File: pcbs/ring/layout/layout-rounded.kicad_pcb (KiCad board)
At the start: 2 copper layers, 59.8 x 6.2 mm, 61 parts, among them J1 ?, Q1 CSD13380F3T, Q2 CSD13380F3T, U1 BQ27427YZFR, U2 BQ29700, U3 nRF52833-QDAA, U4 MAX30102EFD+T, U5 LSM6DSOX, U6 TMP117AIDRVR, U7 TPS7A2018PDQN, Y1 32MHz, Y2 32.768kHz

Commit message: rounded
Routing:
- net swdclk: track 46.0 -> 44.9 mm
- net swdio: track 37.4 -> 36.7 mm
- net cpu.dec4_6: track 18.2 -> 17.7 mm

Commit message: more vias
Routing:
- net GND: vias 50 -> 55

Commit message: cleanup
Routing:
- net GND: vias 55 -> 56
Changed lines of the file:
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@@
 	)
 	(via
+		(at 173.85 84.55)
+		(size 0.35)
+		(drill 0.15)
+		(layers "F.Cu" "B.Cu")
+		(free yes)
+		(net 2)
+	)
+	(via
 		(at 145.3 85.35)
 		(size 0.35)
@@
 	)
 	(segment
-		(start 139.172615 81.872615)
-		(end 138.673743 81.373743)
-		(width 0.125)
-		(layer "B.Cu")
-		(net 27)
-	)
-	(segment
 		(start 142.9 82.3)
 		(end 143.143933 82.3)
@@
 	)
 	(segment
-		(start 140.524819 83.2)
+		(start 139.172615 81.872615)
+		(end 138.673743 81.373743)
+		(width 0.125)
+		(layer "B.Cu")
+		(net 27)
+	)
+	(segment
+		(start 141.047805 83.2)
 		(end 141.075 83.2)
 		(width 0.125)
@@
 	)
 	(segment
-		(start 142.302512 82.547487)
-		(end 142.056586 82.793413)
+		(start 139.175385 81.879299)
+		(end 139.172615 81.872615)
 		(width 0.125)
 		(layer "B.Cu")
@@
 	)
 	(segment
-		(start 140.48245 83.18245)
-		(end 140.466283 83.166283)
+		(start 140.10596 82.809874)
+		(end 139.175385 81.879299)
+		(width 0.125)
+		(layer "B.Cu")
+		(net 27)
+	)
+	(segment
+		(start 142.302512 82.547487)
+		(end 142.056507 82.793492)
 		(width 0.125)
 		(layer "B.Cu")
@@
 		(net 27)
 	)
-	(segment
-		(start 140.459602 83.163516)
-		(end 139.175385 81.879299)
-		(width 0.125)
-		(layer "B.Cu")
-		(net 27)
-	)
-	(arc
-		(start 139.174 81.875957)
-		(mid 139.17436 81.877765)
-		(end 139.175385 81.879299)
-		(width 0.125)
-		(layer "B.Cu")
-		(net 27)
-	)
 	(arc
 		(start 147.84205 82.69205)
@@
 	)
 	(arc
-		(start 142.056586 82.793413)
-		(mid 141.60623 83.094331)
+		(start 142.056507 82.793492)
+		(mid 141.606238 83.094352)
 		(end 141.075 83.2)
 		(width 0.125)
@@
 	)
 	(arc
-		(start 140.459602 83.163516)
-		(mid 140.461134 83.16454)
-		(end 140.462943 83.1649)
-		(width 0.125)
-		(layer "B.Cu")
-		(net 27)
-	)
-	(arc
 		(start 153.077328 83.2341)
 		(mid 153.175973 83.253722)
@@
 	)
 	(arc
-		(start 138.55 81.075)
-		(mid 138.582159 81.236678)
-		(end 138.673743 81.373743)
-		(width 0.125)
-		(layer "B.Cu")
-		(net 27)
-	)
-	(arc
 		(start 164.749479 82.999479)
 		(mid 165.082351 83.221897)
@@
 	)
 	(arc
-		(start 140.48245 83.18245)
-		(mid 140.501889 83.195438)
-		(end 140.524819 83.2)
+		(start 140.10596 82.809874)
+		(mid 140.538082 83.098609)
+		(end 141.047805 83.2)
 		(width 0.125)
 		(layer "B.Cu")
@@
 	)
 	(arc
-		(start 140.466283 83.166283)
-		(mid 140.46475 83.165259)
-		(end 140.462943 83.1649)
-		(width 0.125)
-		(layer "B.Cu")
-		(net 27)
-	)
-	(arc
-		(start 139.172615 81.872615)
-		(mid 139.17364 81.874148)
-		(end 139.174 81.875957)
+		(start 138.673743 81.373743)
+		(mid 138.582159 81.236678)
+		(end 138.55 81.075)
 		(width 0.125)
 		(layer "B.Cu")

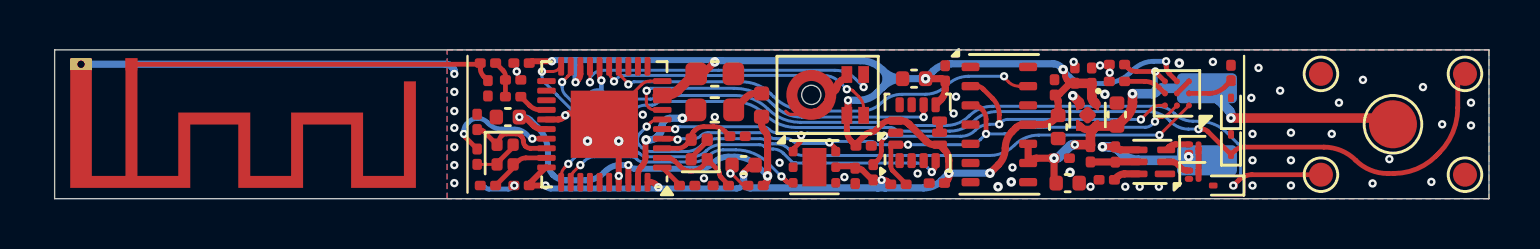
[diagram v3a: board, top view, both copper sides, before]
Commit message: two-sided port
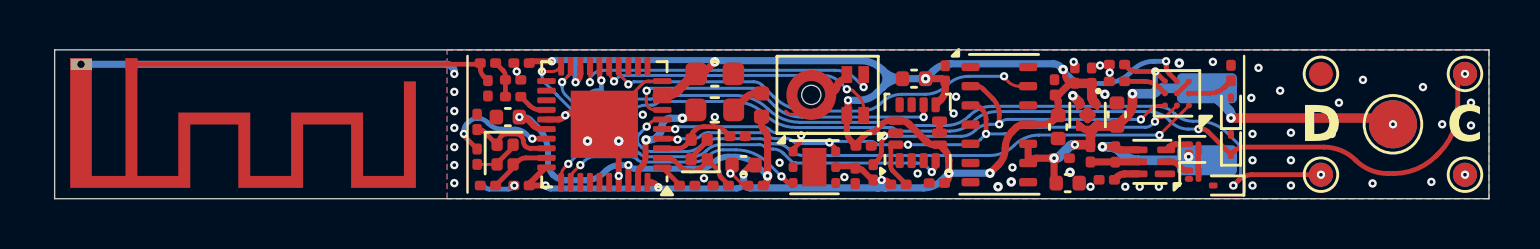
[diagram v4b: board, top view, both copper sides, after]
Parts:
- added TP10: , TestPoint_Pad_D1.0mm:TestPoint_Pad_D1.0mm, B.Cu at (171.0, 85.2)
- added TP2: , TestPoint_Pad_D1.0mm:TestPoint_Pad_D1.0mm, B.Cu at (177.0, 81.0)
- added TP8: , TestPoint_Pad_D2.0mm:TestPoint_Pad_D2.0mm, B.Cu at (174.0, 83.1)
- added TP9: , TestPoint_Pad_D1.0mm:TestPoint_Pad_D1.0mm, B.Cu at (177.0, 85.2)
- renumbered TP2 to TP3, TP3 to TP4, TP4 to TP5, TP5 to TP6, TP6 to TP7
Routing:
- net swdclk: track 44.7 -> 44.8 mm, vias 2 -> 3
- net swdio: vias 2 -> 3
- net VBATT: vias 5 -> 6
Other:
- board text added: "C"
- board text added: "D"

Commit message: change port spacing
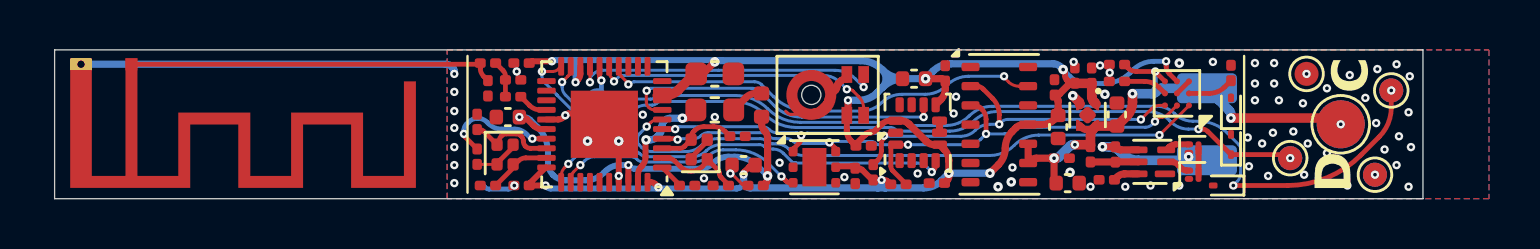
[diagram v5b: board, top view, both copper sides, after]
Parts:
- moved TP2 8.08 mm to (169.7, 84.5)
- moved TP5 8.08 mm to (169.7, 84.5)
- moved TP10 4.57 mm to (173.9, 81.7)
- moved TP4 4.57 mm to (173.9, 81.7)
- moved TP6 3.75 mm to (173.2, 85.2)
- moved TP9 3.75 mm to (173.2, 85.2)
- moved TP3 2.18 mm to (171.8, 83.1)
- moved TP8 2.18 mm to (171.8, 83.1)
- moved TP7 0.60 mm to (170.4, 81.0)
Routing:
- net swdclk: track 44.8 -> 34.7 mm
- net swdio: track 36.6 -> 41.6 mm
- net GND: track 35.5 -> 32.5 mm, vias 56 -> 69
- net VBATT: track 23.3 -> 21.1 mm
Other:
- board size 59.8 x 6.2 mm -> 57 x 6.2 mm

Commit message: cleanup
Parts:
- moved BT1 0.25 mm to (166.0, 83.1)
- moved C1 0.25 mm to (162.3, 80.6)
- moved C10 0.25 mm to (145.8, 85.7)
- moved C11 0.25 mm to (146.4, 83.6)
- moved C12 0.25 mm to (144.3, 85.7)
- moved C13 0.25 mm to (135.6, 84.5)
- moved C14 0.25 mm to (136.9, 82.8)
- moved C15 0.25 mm to (147.2, 85.7)
- moved C16 0.25 mm to (137.1, 81.2)
- moved C17 0.25 mm to (136.1, 81.6)
- moved C18 0.25 mm to (160.2, 85.5)
- moved C19 0.25 mm to (160.0, 84.5)
- moved C2 0.25 mm to (162.3, 81.3)
- moved C20 0.25 mm to (159.8, 83.2)
- moved C21 0.25 mm to (159.7, 81.6)
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
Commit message: update rounded board
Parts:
- removed D2, D3: ESD9B5.0ST5G, D_SOD-923:D_SOD-923
- removed TP10: , TestPoint_Pad_D1.0mm:TestPoint_Pad_D1.0mm
- removed the TP2 at (169.5, 84.5)
- removed the TP4 at (173.7, 81.7)
- removed the TP5 at (169.5, 84.5)
- added U6: ?, PinHeader_1x03_P1.00mm_Vertical_SMD_Pin1Left:PinHeader_1x03_P1.00mm_Vertical_SMD_Pin1Left, B.Cu at (140.8, 83.0)
- moved TP1 6.66 mm to (147.2, 82.4)
- moved BT1 0.25 mm to (166.3, 83.1)
- moved C1 0.25 mm to (162.5, 80.6)
- moved C10 0.25 mm to (146.0, 85.7)
- moved C11 0.25 mm to (146.7, 83.6)
- moved C12 0.25 mm to (144.6, 85.7)
- moved C13 0.25 mm to (135.8, 84.5)
- moved C14 0.25 mm to (137.1, 82.8)
- moved C15 0.25 mm to (147.4, 85.7)
- moved C16 0.25 mm to (137.3, 81.2)
- moved C17 0.25 mm to (136.3, 81.6)
- moved C18 0.25 mm to (160.4, 85.5)
- moved C19 0.25 mm to (160.2, 84.5)
- moved C2 0.25 mm to (162.5, 81.3)
- moved C20 0.25 mm to (160.1, 83.2)
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- renumbered TP3 to TP2, TP6 to TP3, TP7 to TP4, TP8 to TP5, TP9 to TP6, U6 to U7, U7 to U8
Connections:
- U3 pad 31: imu_int1 -> tmp_int
- U3 pad 32: tmp_int -> imu_int1
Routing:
- net swdio: track 41.6 -> 1.19 mm, vias 3 -> 1
- net swdclk: track 34.7 -> 4.55 mm, vias 3 -> 1
- net rst: track 1.50 -> 7.18 mm
- net GND: track 32.5 -> 35.6 mm, vias 69 -> 68
- net tmp_int: track 10.5 -> 11.1 mm
- net imu_int1: track 17.3 -> 16.8 mm
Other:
- board size 57 x 6.2 mm -> 56 x 6.2 mm
- board text removed: "C"
- board text removed: "D"
